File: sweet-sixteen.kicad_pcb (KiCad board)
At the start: 2 copper layers, 99.5 x 104.5 mm, 83 parts, among them P1 SDA_I, P10 VIN_O, P11 GND_O, P12 SDA_O, P13 CLK_O, P14 LE_O, P15 ~OE_O, P2 CLK_I, P3 LE_I, P4 ~OE_I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

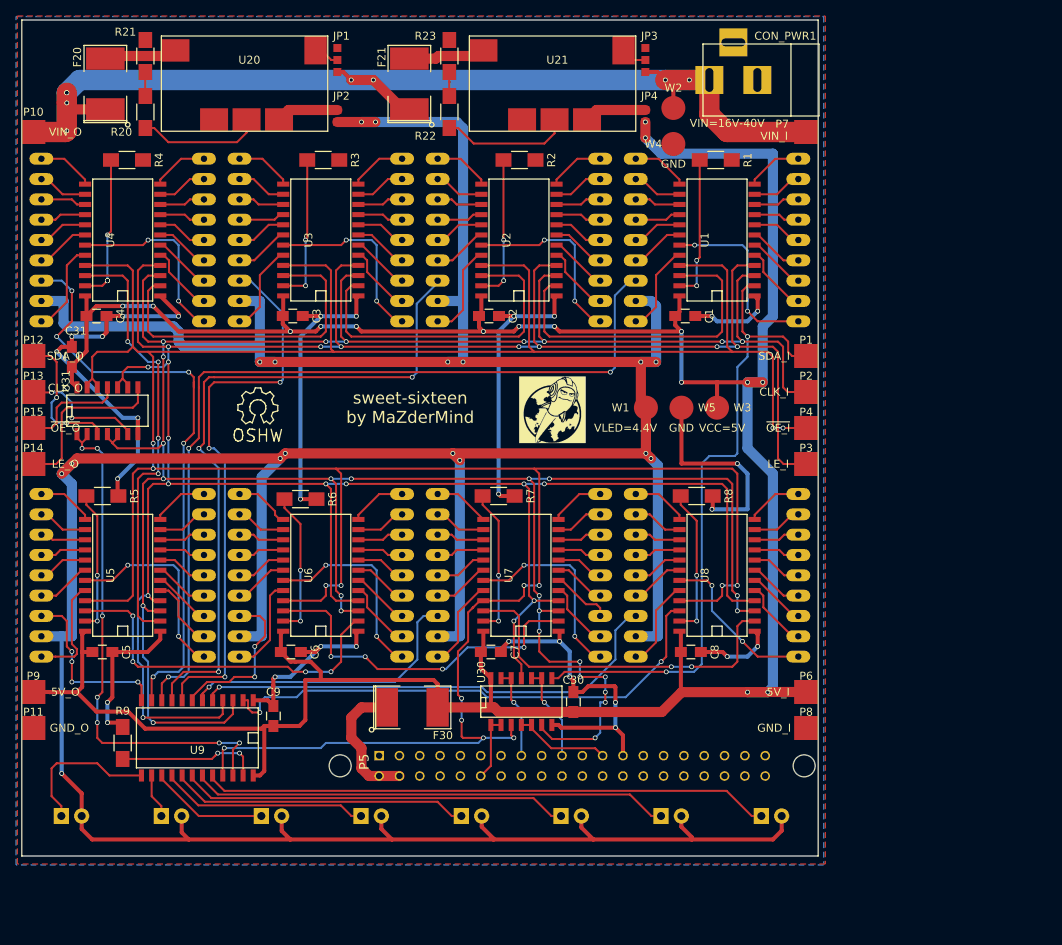
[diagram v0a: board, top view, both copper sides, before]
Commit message: move chaining-pads to new outline, position pcb in a well described location on paper, fix outline to be on mm boundaries
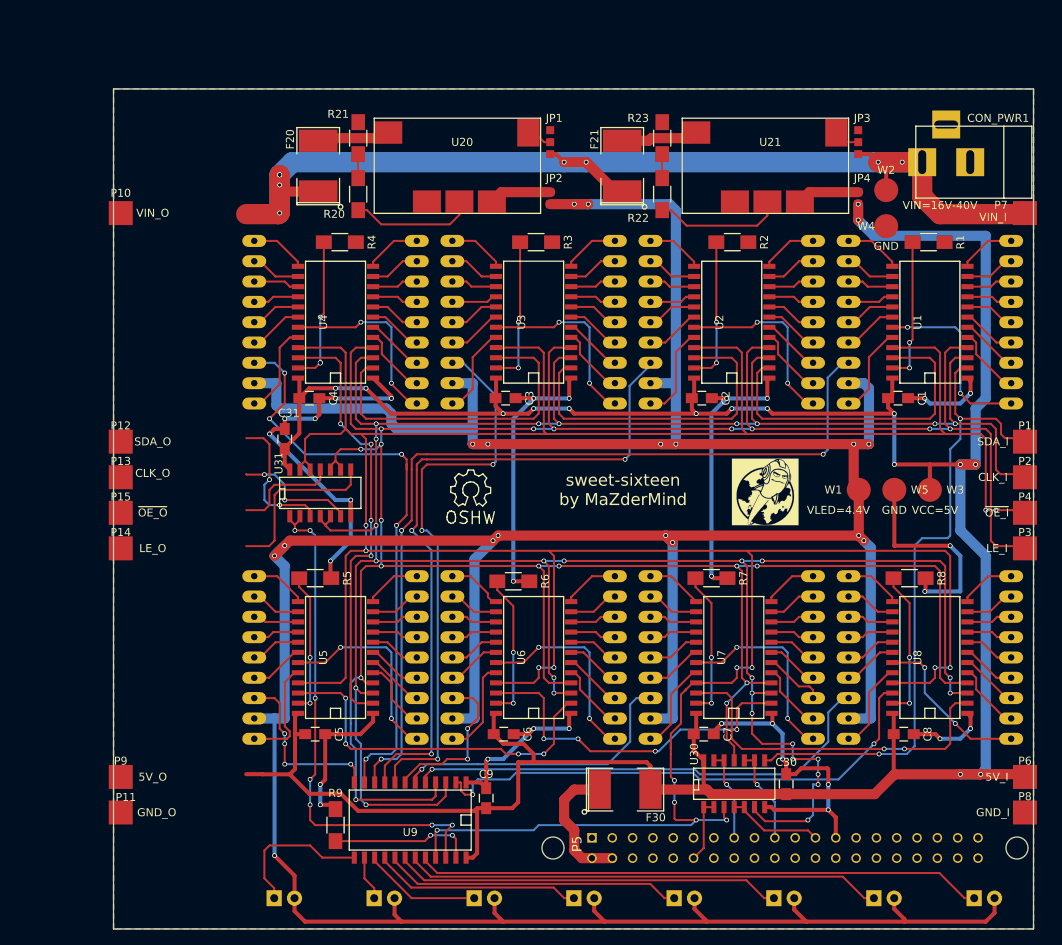
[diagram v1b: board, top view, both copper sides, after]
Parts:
- moved P1 29.4 mm to (213.9, 94.1)
- moved P2 29.4 mm to (213.9, 98.5)
- moved P6 29.3 mm to (213.9, 136.0)
- moved P4 29.3 mm to (213.9, 103.0)
- moved P8 29.3 mm to (213.9, 140.4)
- moved P3 29.3 mm to (213.9, 107.4)
- moved P7 29.2 mm to (213.9, 65.5)
- moved AFF7 28.5 mm to (177.3, 121.1)
- moved F30 28.5 mm to (163.9, 137.6)
- moved U7 28.5 mm to (177.5, 121.1)
- moved W1 28.5 mm to (193.2, 100.1)
- moved W5 28.5 mm to (197.6, 100.1)
- moved ? 28.5 mm to (144.6, 100.1)
- moved AFF2 28.5 mm to (177.3, 79.2)
- moved AFF5 28.5 mm to (127.7, 121.1)
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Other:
- board size 99.5 x 104.5 mm -> 115 x 105 mm

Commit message: reposition everything, rip up everything… meeeh…
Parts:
- moved G*** 23.5 mm to (158.0, 100.4)
- moved ? 16.7 mm to (128.0, 99.0)
- moved R4 16.3 mm to (112.0, 69.0)
- moved F20 15.6 mm to (110.0, 59.0)
- moved C31 14.8 mm to (108.0, 100.0)
- moved C5 14.2 mm to (111.0, 131.0)
- moved R21 13.6 mm to (117.0, 55.0)
- moved C4 13.5 mm to (111.0, 89.0)
- moved AFF4 13.2 mm to (114.5, 79.0)
- moved U4 13.2 mm to (114.5, 79.0)
- moved AFF5 13.2 mm to (114.5, 121.0)
- moved U5 13.2 mm to (114.5, 121.0)
- moved R5 13.2 mm to (112.0, 111.0)
- moved D1 12.9 mm to (107.2, 150.1), turned to 270 degrees
- moved R3 11.8 mm to (141.0, 69.0)
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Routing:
- net /VLED: track 485.2 -> 0.00 mm, vias 17 -> 0
- net /~OE: track 416.7 -> 0.00 mm, vias 15 -> 0
- net VCC: track 370.2 -> 0.00 mm, vias 16 -> 0
- net /CLK: track 363.9 -> 0.00 mm, vias 29 -> 0
- net /LE: track 356.7 -> 0.00 mm, vias 19 -> 0
- net GND: track 247.0 -> 0.00 mm, vias 29 -> 0
- net VIN: track 140.5 -> 0.00 mm, vias 8 -> 0
- net Net-(AFF1-Pad12): track 108.3 -> 0.00 mm, vias 3 -> 0
- net Net-(AFF2-Pad12): track 85.7 -> 0.00 mm, vias 3 -> 0
- net /SDA_I: track 81.5 -> 0.00 mm, vias 2 -> 0
- net Net-(AFF4-Pad12): track 74.8 -> 0.00 mm, vias 5 -> 0
- net Net-(D8-Pad1): track 71.0 -> 0.00 mm
- net Net-(AFF3-Pad12): track 70.6 -> 0.00 mm, vias 3 -> 0
- net /SDA_89: track 65.4 -> 0.00 mm, vias 2 -> 0
- net /SDA_O: track 64.5 -> 0.00 mm, vias 7 -> 0
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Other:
- board size 115 x 105 mm -> 116 x 105 mm

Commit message: re-route things with more care
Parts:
- moved P14 5.00 mm to (101.5, 102.5)
- moved P15 5.00 mm to (101.5, 107.5)
- moved P4 5.00 mm to (214.5, 107.5)
- moved P3 4.92 mm to (214.5, 102.5)
- moved W5 4.60 mm to (193.0, 100.0)
- moved W1 4.15 mm to (189.0, 100.0)
- moved R20 4.00 mm to (117.0, 63.0)
- moved R22 4.00 mm to (166.0, 63.0)
- moved W3 2.94 mm to (200.0, 98.0)
- moved U9 2.00 mm to (139.0, 141.0)
- turned C31 to 270 degrees
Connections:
- net /SD23 renamed /SD_23
- net Net-(P13-Pad1) renamed /CLK_O
- net Net-(P14-Pad1) renamed /LE_O
- net Net-(P15-Pad1) renamed /~OE_O
- P12 pad 1: Net-(P12-Pad1) -> /SDA_O
- U31 pad 1: /SDA_O -> /SDA_9O
- U31 pad 2: /SDA_O -> /SDA_9O
- U31 pad 3: Net-(P12-Pad1) -> /SDA_O
- U9 pad 22: /SDA_O -> /SDA_9O
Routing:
- net VCC: track 0.00 -> 369.1 mm, vias 0 -> 4
- net /~OE: track 0.00 -> 303.9 mm, vias 0 -> 9
- net /LE: track 0.00 -> 296.2 mm, vias 0 -> 6
- net /CLK: track 0.00 -> 294.5 mm, vias 0 -> 9
- net VIN: track 0.00 -> 160.0 mm, vias 0 -> 6
- net /VLED: track 0.00 -> 101.5 mm
- net Net-(D8-Pad1): track 0.00 -> 69.9 mm
- net Net-(D7-Pad1): track 0.00 -> 56.7 mm
- net Net-(D6-Pad1): track 0.00 -> 43.5 mm
- net /SD_23: track 0.00 -> 32.8 mm
- net /SDA_12: track 0.00 -> 32.8 mm
- net /SDA_34: track 0.00 -> 32.8 mm
- net Net-(D5-Pad1): track 0.00 -> 30.3 mm
- net Net-(D1-Pad1): track 0.00 -> 26.6 mm
- net Net-(AFF3-Pad9): track 0.00 -> 22.7 mm, vias 0 -> 1
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
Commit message: re-route all
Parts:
- moved ? 59.0 mm to (187.0, 99.0)
- moved W1 31.2 mm to (158.0, 96.5)
- moved G*** 23.0 mm to (135.0, 101.5)
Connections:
- U9 pad 10: Net-(AFF1-Pad12) -> Net-(AFF3-Pad12)
- U9 pad 8: Net-(AFF3-Pad12) -> Net-(AFF1-Pad12)
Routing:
- net /VLED: track 101.5 -> 544.6 mm, vias 0 -> 6
- net GND: track 0.00 -> 234.8 mm, vias 0 -> 36
- net Net-(AFF1-Pad12): track 0.00 -> 119.7 mm, vias 0 -> 2
- net /~OE: track 303.9 -> 405.2 mm, vias 9 -> 13
- net Net-(AFF2-Pad12): track 0.00 -> 92.4 mm, vias 0 -> 2
- net Net-(AFF4-Pad12): track 0.00 -> 83.2 mm, vias 0 -> 2
- net /SDA_89: track 0.00 -> 82.2 mm, vias 0 -> 2
- net /SDA_9O: track 0.00 -> 76.7 mm, vias 0 -> 6
- net /SDA_I: track 17.3 -> 92.9 mm, vias 0 -> 4
- net /SDA_45: track 0.44 -> 69.1 mm, vias 0 -> 4
- net Net-(AFF8-Pad12): track 0.00 -> 62.8 mm, vias 0 -> 4
- net Net-(AFF3-Pad12): track 0.00 -> 61.1 mm
- net /SDA_56: track 0.44 -> 60.7 mm, vias 0 -> 2
- net /SDA_78: track 0.00 -> 49.0 mm, vias 0 -> 2
- net Net-(AFF5-Pad12): track 0.00 -> 46.9 mm, vias 0 -> 2
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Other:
- net class Default: clearance 0.2 -> 0.254; trace_width 0.25 -> 0.254
- rule trace_clearance: 0.2 -> 0.254
- rule trace_min: 0.2 -> 0.254
- board text added: "https://github.com/MaZderMind/sweet-sixteen"
